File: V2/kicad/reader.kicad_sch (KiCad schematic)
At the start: 88 parts, among them SW1 SSSS812201, U1 MLD-TF PUSH-H18, U2 MAX98357AETE+T, U3 MCP16301Hx-xCH, U4 TCAN1057AVDRQ1, U5 RJ-064-1, U6 STM32H523CET6, U7 ESD2CAN24-ES, Y1 16MHz

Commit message: in process of making pcb
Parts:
- removed R5: 560 R, Resistor_SMD:R_0603_1608Metric, symbol Device:R
- removed RC522: RFID RC522, UACS:PinSocket_1x08_P2.54mm_Vertical, symbol Connector:Conn_01x08_Socket
- removed SP_Conn1: P=1.25mm, easyeda2kicad:CONN-TH_530480210, symbol easyeda2kicad:530480210
- added R15: 560 R, Resistor_SMD:R_0402_1005Metric, symbol Device:R
- added RC1: RFID RC522, UACS:PinSocket_1x08_P2.54mm_Vertical, symbol easyeda2kicad:HXPM2.54-1X8PZCH11
- added SP_Conn1: P=1.25mm, easyeda2kicad:CONN-TH_0530470210, symbol easyeda2kicad:0530470210
- SW1: value SSSS812201 -> SW_Rezistance
- SW2: renamed from BOOT2; value SW2 -> SW_src
- TP3: renamed from WS; value TestPoint -> WS
- U1: renamed from U6; footprint LQFP48_STM -> STM32H523CET6:LQFP48_STM
- renumbered BOOT1 to BOOT2, C30 to C10, C29 to C11, C28 to C12, C7 to C13, C36 to C14, C37 to C15, C3 to C16, C2 to C17, C35 to C18, C34 to C19, C4 to C2, C33 to C20, C23 to C21, C14 to C22, C12 to C23, C15 to C24, C17 to C25, C16 to C3, C6 to C4, C13 to C5, C8 to C6, C5 to C7, C32 to C8, C31 to C9, D7 to D1, D6 to D2, D10 to D3, D9 to D4, D1 to D5, D3 to D6, D5 to D7, D4 to D8, D2 to D9, FB2 to FB1, R17 to R1, R23 to R10, R24 to R11, R26 to R12, R11 to R13, R4 to R14, R6 to R16, R7 to R17, R8 to R18, R12 to R19, R20 to R2, R13 to R20, R9 to R21, R19 to R3, R14 to R4, R15 to R5, R16 to R6, R10 to R7, R21 to R8, R22 to R9, TP9 to TP1, TP7 to TP2, TP6 to TP4, TP3 to TP5, TP2 to TP6, TP1 to TP7, TP4 to TP8, TP5 to TP9, U1 to U3, U7 to U5, U5 to U6, U3 to U7
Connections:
- net +3.3V: now also RC1.1
- net GND: now also USB-C1.SH (SHIELD), RC1.3; no longer USB-C1.S1 (SHIELD)
- net LED_G2: now also U1.40 (PB4); no longer U1.42 (PB6)
- net LED_R1: now also R15.1
- net LED_R2: now also U1.38 (PA15); no longer U1.41 (PB5)
- net RFID_IRQ: now also RC1.4
- net RFID_SS: now also RC1.8
- net SPI_MISO: now also RC1.5
- net SPI_MOSI: now also RC1.6
- net SPI_SCK: now also RC1.7
- net at Speaker1.1, U2.10 (OUTN): now also SP_Conn1.1
- net at Speaker1.2, U2.9 (OUTP): now also SP_Conn1.2
- net RFID_RST: now reaches U1.21 (PB10)
- net RFID_RST: now also RC1.2
- net at LED1.1 (A1): now also R15.2
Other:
- note added: "Warning: No net found for component SW1 pad 5 (no pin 5 in symbol). Warning: No net found for component USB-C1 pad B8 (no pin B8 in symbol). Warning: No net found for component SW1 pad 7 (no pin 7 in symbol). Warning: No net found for component SW1 pad 6 (no pin 6 in symbol). Warning: No net found for component SW1 pad 8 (no pin 8 in symbol). Warning: No net found for component USB-C1 pad A8 (no 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"

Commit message: pcb propably dones
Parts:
- added H4: MountingHole, MountingHole:ToolingHole_1.152mm, symbol Mechanical:MountingHole
- C1, C10, C11, C12, C13, C18, C19, C2, C20, C21, C22, C23, C24, C25, C3, C5, C6, C8, C9, FB1, R12, R13, R14, R15, R16, R17, R18, R19, R2, R20, R21, R3, R5, R6, R7: KiLib_Generator (none) -> SMD_2terminal_chip_molded
- RC1: JLCPCB (none) -> https://jlcpcb.com/partdetail/28187-2_54_1_8P/C27438; LCSC (none) -> C27438
- SW1: LCSC Part (none) -> C160878
- TP1, TP2, TP3, TP4, TP5: footprint (none) -> UACS:TestPoint_Drill-1mm
- TP6, TP7, TP8, TP9: footprint TestPoint:TestPoint_THTPad_D1.0mm_Drill0.5mm -> UACS:TestPoint_Drill-1mm; now in the parts list
- U7: KiLib_Generator (none) -> package/gullwing
- Y1: KiLib_Generator (none) -> crystal_resonator_oscillator
- renumbered BOOT2 to BOOT1, SP_Conn1 to SP_Con1
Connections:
- net LED_G1: now also U1.40 (PB4); no longer U1.12 (PA2)
- net LED_G2: now also U1.42 (PB6); no longer U1.40 (PB4)
- net LED_R1: now also U1.38 (PA15); no longer U1.11 (PA1)
- net LED_R2: now also U1.41 (PB5); no longer U1.38 (PA15)
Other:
- note removed: "Warning: No net found for component SW1 pad 5 (no pin 5 in symbol). Warning: No net found for component USB-C1 pad B8 (no pin B8 in symbol). Warning: No net found for component SW1 pad 7 (no pin 7 in symbol). Warning: No net found for component SW1 pad 6 (no pin 6 in symbol). Warning: No net found for component SW1 pad 8 (no pin 8 in symbol). Warning: No net found for component USB-C1 pad A8 (no 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"

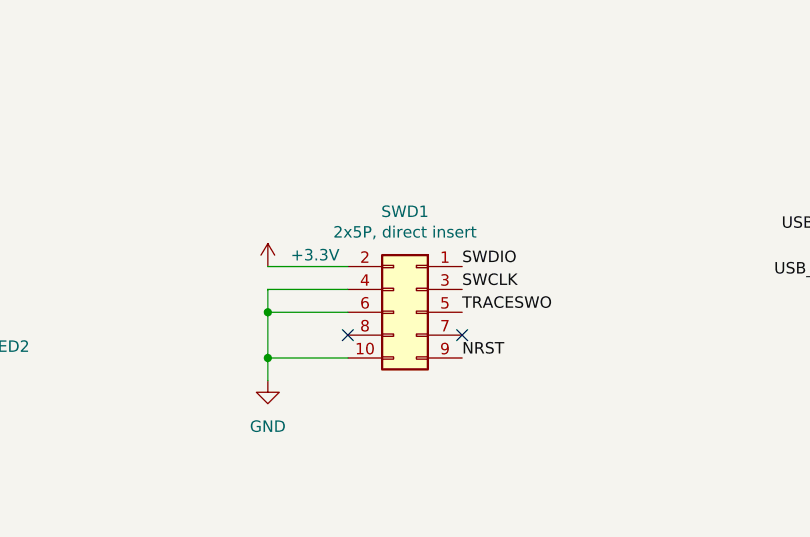
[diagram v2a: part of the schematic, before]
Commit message: changed debug connector to male, fixed 3d models not showing, moved sdcard slot invards by 2.3mm
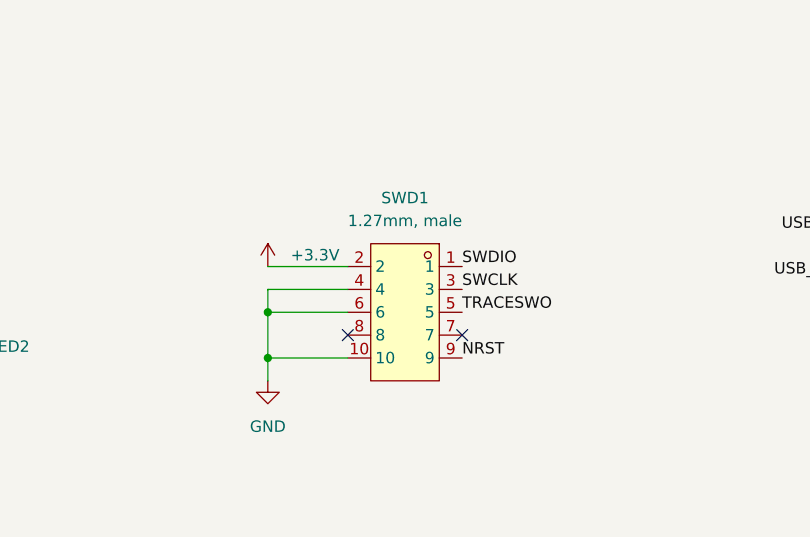
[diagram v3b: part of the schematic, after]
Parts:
- removed SWD1: 2x5P, direct insert, UACS:PinSocket_2x05_P1.27mm_Vertical, symbol Connector_Generic:Conn_02x05_Odd_Even
- added SWD1: 1.27mm, male, easyeda2kicad:CONN-TH_IDC1.27-UP1S-5A, symbol easyeda2kicad:IDC1.27-UP1S-5A
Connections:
- net +3.3V: now also SWD1.2
- net GND: now also SWD1.10, SWD1.4, SWD1.6
- net NRST: now also SWD1.9
- net SWCLK: now also SWD1.3
- net SWDIO: now also SWD1.1
- net TRACESWO: now also SWD1.5
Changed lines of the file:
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@@
+	)
+	(symbol
+		(lib_id "easyeda2kicad:IDC1.27-UP1S-5A")
+		(at 95.25 256.54 0)
+		(mirror y)
+		(unit 1)
+		(body_style 1)
+		(exclude_from_sim no)
+		(in_bom yes)
+		(on_board yes)
+		(in_pos_files yes)
+		(dnp no)
+		(fields_autoplaced yes)
+		(property "Reference" "SWD1"
+			(at 95.25 243.84 0)
+			(show_name no)
+			(do_not_autoplace no)
+			(effects
+				(font
+					(size 1.27 1.27)
+				)
+			)
+		)
+		(property "Value" "1.27mm, male"
+			(at 95.25 246.38 0)
+			(show_name no)
+			(do_not_autoplace no)
+			(effects
+				(font
+					(size 1.27 1.27)
+				)
+			)
+		)
+		(property "Footprint" "easyeda2kicad:CONN-TH_IDC1.27-UP1S-5A"
+			(at 95.25 269.24 0)
+			(hide yes)
+			(show_name no)
+			(do_not_autoplace no)
+			(effects
+				(font
+					(size 1.27 1.27)
+				)
+			)
+		)
+		(property "Datasheet" "https://www.lcsc.com/datasheet/C22392234.pdf"
+			(at 95.25 271.78 0)
+			(hide yes)
+			(show_name no)
+			(do_not_autoplace no)
+			(effects
+				(font
+					(size 1.27 1.27)
+				)
+			)
+		)
+		(property "Description" ""
+			(at 95.25 256.54 0)
+			(hide yes)
+			(show_name no)
+			(do_not_autoplace no)
+			(effects
+				(font
+					(size 1.27 1.27)
+				)
+			)
+		)
+		(property "Manufacturer" "XYECONN(辛译)"
+			(at 95.25 274.32 0)
+			(hide yes)
+			(show_name no)
+			(do_not_autoplace no)
+			(effects
+				(font
+					(size 1.27 1.27)
+				)
+			)
+		)
+		(property "MPN" "IDC1.27-UP1S-5A"
+			(at 95.25 276.86 0)
+			(hide yes)
+			(show_name no)
+			(do_not_autoplace no)
+			(effects
+				(font
+					(size 1.27 1.27)
+				)
+			)
+		)
+		(property "LCSC Part" "C22392234"
+			(at 95.25 279.4 0)
+			(hide yes)
+			(show_name no)
+			(do_not_autoplace no)
+			(effects
+				(font
+					(size 1.27 1.27)
+				)
+			)
+		)
+		(pin "2"
+		)
+		(pin "1"
+		)
+		(pin "7"
+		)
+		(pin "3"
+		)
+		(pin "5"
+		)
+		(pin "4"
+		)
+		(pin "8"
+		)
+		(pin "10"
+		)
+		(pin "6"
+		)
+		(pin "9"
+		)
+		(instances
+			(project "reader"
+				(path "/6275a1a7-d424-4390-b849-2e49b1a9780b"
+					(reference "SWD1")
+					(unit 1)
+				)
+			)
+		)
 	)
 	(symbol
@@
 					(unit 1)
 				)
-			)
-		)
-	)
-	(symbol
-		(lib_id "Connector_Generic:Conn_02x05_Odd_Even")
-		(at 96.52 256.54 0)
-		(mirror y)
-		(unit 1)
-		(body_style 1)
-		(exclude_from_sim no)
-		(in_bom yes)
-		(on_board yes)
-		(in_pos_files yes)
-		(dnp no)
-		(property "Reference" "SWD1"
-			(at 95.25 245.364 0)
-			(show_name no)
-			(do_not_autoplace no)
-			(effects
-				(font
-					(size 1.27 1.27)
-				)
-			)
-		)
-		(property "Value" "2x5P, direct insert"
-			(at 95.25 247.65 0)
-			(show_name no)
-			(do_not_autoplace no)
-			(effects
-				(font
-					(size 1.27 1.27)
-				)
-			)
-		)
-		(property "Footprint" "UACS:PinSocket_2x05_P1.27mm_Vertical"
-			(at 96.52 256.54 0)
-			(hide yes)
-			(show_name no)
-			(do_not_autoplace no)
-			(effects
-				(font
-					(size 1.27 1.27)
-				)
-			)
-		)
-		(property "Datasheet" "https://jlcpcb.com/api/file/downloadByFileSystemAccessId/8588891463094841344"
-			(at 96.52 256.54 0)
-			(hide yes)
-			(show_name no)
-			(do_not_autoplace no)
-			(effects
-				(font
-					(size 1.27 1.27)
-				)
-			)
-		)
-		(property "Description" "Generic connector, double row, 02x05, odd/even pin numbering scheme (row 1 odd numbers, row 2 even numbers), script generated (kicad-library-utils/schlib/autogen/connector/)"
-			(at 96.52 256.54 0)
-			(hide yes)
-			(show_name no)
-			(do_not_autoplace no)
-			(effects
-				(font
-					(size 1.27 1.27)
-				)
-			)
-		)
-		(property "Note" ""
-			(at 96.52 256.54 0)
-			(hide yes)
-			(show_name no)
-			(do_not_autoplace no)
-			(effects
-				(font
-					(size 1.27 1.27)
-				)
-			)
-		)
-		(property "JLCPCB" "https://jlcpcb.com/partdetail/Hoauc-2343U205CNG1SNT01/C350287"
-			(at 96.52 256.54 0)
-			(hide yes)
-			(show_name no)
-			(do_not_autoplace no)
-			(effects
-				(font
-					(size 1.27 1.27)
-				)
-			)
-		)
-		(property "LCSC" "C350287"
-			(at 96.52 256.54 0)
-			(hide yes)
-			(show_name no)
-			(do_not_autoplace no)
-			(effects
-				(font
-					(size 1.27 1.27)
-				)
-			)
-		)
-		(property "Field5" ""
-			(at 96.52 256.54 0)
-			(hide yes)
-			(show_name no)
-			(do_not_autoplace no)
-			(effects
-				(font
-					(size 1.27 1.27)
-				)
-			)
-		)
-		(property "Field6" ""
-			(at 96.52 256.54 0)
-			(hide yes)
-			(show_name no)
-			(do_not_autoplace no)
-			(effects
-				(font
-					(size 1.27 1.27)
-				)
-			)
-		)
-		(pin "5"
-		)
-		(pin "2"
-		)
-		(pin "1"
-		)
-		(pin "6"
-		)
-		(pin "3"
-		)
-		(pin "4"
-		)
-		(pin "9"
-		)
-		(pin "7"
-		)
-		(pin "8"
-		)
-		(pin "10"
-		)
-		(instances
-			(project "reader"
-				(path "/6275a1a7-d424-4390-b849-2e49b1a9780b"
-					(reference "SWD1")
-					(unit 1)
-				)

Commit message: final touches
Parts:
- removed H4: MountingHole, MountingHole:ToolingHole_1.152mm, symbol Mechanical:MountingHole
- removed SWD1: 1.27mm, male, easyeda2kicad:CONN-TH_IDC1.27-UP1S-5A, symbol easyeda2kicad:IDC1.27-UP1S-5A
- added SWD1: 1.27mm, male, easyeda2kicad:IDC-TH_10P-P1.27-X1270WV-2X05A-6TV01, symbol easyeda2kicad:X1270WV-2X05B-6TV01
- renumbered SP_Con1 to Speaker2
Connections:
- net +3.3V: now also SWD1.2
- net GND: now also SWD1.10, SWD1.4, SWD1.6
- net NRST: now also SWD1.9
- net SWCLK: now also SWD1.3
- net SWDIO: now also SWD1.1
- net TRACESWO: now also SWD1.5
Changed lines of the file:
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@@
 	)
 	(symbol
-		(lib_id "Mechanical:MountingHole")
-		(at 137.16 186.69 0)
-		(mirror y)
-		(unit 1)
-		(body_style 1)
-		(exclude_from_sim yes)
-		(in_bom no)
-		(on_board yes)
-		(in_pos_files yes)
-		(dnp no)
-		(property "Reference" "H4"
-			(at 134.62 185.4199 0)
-			(show_name no)
-			(do_not_autoplace no)
-			(effects
-				(font
-					(size 1.27 1.27)
-				)
-				(justify left)
-			)
-		)
-		(property "Value" "MountingHole"
-			(at 134.62 187.9599 0)
-			(show_name no)
-			(do_not_autoplace no)
-			(effects
-				(font
-					(size 1.27 1.27)
-				)
-				(justify left)
-			)
-		)
-		(property "Footprint" "MountingHole:ToolingHole_1.152mm"
-			(at 137.16 186.69 0)
-			(hide yes)
-			(show_name no)
-			(do_not_autoplace no)
-			(effects
-				(font
-					(size 1.27 1.27)
-				)
-			)
-		)
-		(property "Datasheet" ""
-			(at 137.16 186.69 0)
-			(hide yes)
-			(show_name no)
-			(do_not_autoplace no)
-			(effects
-				(font
-					(size 1.27 1.27)
-				)
-			)
-		)
-		(property "Description" "Mounting Hole without connection"
-			(at 137.16 186.69 0)
-			(hide yes)
-			(show_name no)
-			(do_not_autoplace no)
-			(effects
-				(font
-					(size 1.27 1.27)
-				)
-			)
-		)
-		(property "Note" ""
-			(at 137.16 186.69 0)
-			(hide yes)
-			(show_name no)
-			(do_not_autoplace no)
-			(effects
-				(font
-					(size 1.27 1.27)
-				)
-			)
-		)
-		(property "Field5" ""
-			(at 137.16 186.69 0)
-			(hide yes)
-			(show_name no)
-			(do_not_autoplace no)
-			(effects
-				(font
-					(size 1.27 1.27)
-				)
-			)
-		)
-		(property "Field6" ""
-			(at 137.16 186.69 0)
-			(hide yes)
-			(show_name no)
-			(do_not_autoplace no)
-			(effects
-				(font
-					(size 1.27 1.27)
-				)
-			)
-		)
-		(instances
-			(project "reader"
-				(path "/6275a1a7-d424-4390-b849-2e49b1a9780b"
-					(reference "H4")
-					(unit 1)
-				)
-			)
-		)
-	)
-	(symbol
 		(lib_id "power:VAA")
 		(at 187.96 109.22 0)
@@
 	)
 	(symbol
+		(lib_id "easyeda2kicad:X1270WV-2X05B-6TV01")
+		(at 95.25 256.54 0)
+		(mirror y)
+		(unit 1)
+		(body_style 1)
+		(exclude_from_sim no)
+		(in_bom yes)
+		(on_board yes)
+		(in_pos_files yes)
+		(dnp no)
+		(fields_autoplaced yes)
+		(property "Reference" "SWD1"
+			(at 95.25 243.84 0)
+			(show_name no)
+			(do_not_autoplace no)
+			(effects
+				(font
+					(size 1.27 1.27)
+				)
+			)
+		)
+		(property "Value" "1.27mm, male"
+			(at 95.25 246.38 0)
+			(show_name no)
+			(do_not_autoplace no)
+			(effects
+				(font
+					(size 1.27 1.27)
+				)
+			)
+		)
+		(property "Footprint" "easyeda2kicad:IDC-TH_10P-P1.27-X1270WV-2X05A-6TV01"
+			(at 95.25 269.24 0)
+			(hide yes)
+			(show_name no)
+			(do_not_autoplace no)
+			(effects
+				(font
+					(size 1.27 1.27)
+				)
+			)
+		)
+		(property "Datasheet" "https://www.lcsc.com/datasheet/C2962225.pdf"
+			(at 95.25 271.78 0)
+			(hide yes)
+			(show_name no)
+			(do_not_autoplace no)
+			(effects
+				(font
+					(size 1.27 1.27)
+				)
+			)
+		)
+		(property "Description" ""
+			(at 95.25 256.54 0)
+			(hide yes)
+			(show_name no)
+			(do_not_autoplace no)
+			(effects
+				(font
+					(size 1.27 1.27)
+				)
+			)
+		)
+		(property "Manufacturer" "XKB Connection(中国星坤)"
+			(at 95.25 274.32 0)
+			(hide yes)
+			(show_name no)
+			(do_not_autoplace no)
+			(effects
+				(font
+					(size 1.27 1.27)
+				)
+			)
+		)
+		(property "MPN" "X1270WV-2x05B-9TV01"
+			(at 95.25 276.86 0)
+			(hide yes)
+			(show_name no)
+			(do_not_autoplace no)
+			(effects
+				(font
+					(size 1.27 1.27)
+				)
+			)
+		)
+		(property "LCSC Part" "C2962225"
+			(at 95.25 279.4 0)
+			(hide yes)
+			(show_name no)
+			(do_not_autoplace no)
+			(effects
+				(font
+					(size 1.27 1.27)
+				)
+			)
+		)
+		(pin "8"
+		)
+		(pin "5"
+		)
+		(pin "1"
+		)
+		(pin "6"
+		)
+		(pin "3"
+		)
+		(pin "9"
+		)
+		(pin "4"
+		)
+		(pin "7"
+		)
+		(pin "2"
+		)
+		(pin "10"
+		)
+		(instances
+			(project "reader"
+				(path "/6275a1a7-d424-4390-b849-2e49b1a9780b"
+					(reference "SWD1")
+					(unit 1)
+				)
+			)
+		)
+	)
+	(symbol
 		(lib_id "Connector:TestPoint")
 		(at 248.92 270.51 0)
@@
 		(in_pos_files yes)
 		(dnp no)
-		(property "Reference" "SP_Con1"
+		(property "Reference" "Speaker2"
 			(at 354.33 69.596 0)
 			(show_name no)
@@
 			(project "reader"
 				(path "/6275a1a7-d424-4390-b849-2e49b1a9780b"
-					(reference "SP_Con1")
+					(reference "Speaker2")
 					(unit 1)
 				)
@@
 					(unit 1)
 				)
-			)
-		)
-	)
-	(symbol
-		(lib_id "easyeda2kicad:IDC1.27-UP1S-5A")
-		(at 95.25 256.54 0)
-		(mirror y)
-		(unit 1)
-		(body_style 1)
-		(exclude_from_sim no)
-		(in_bom yes)
-		(on_board yes)
-		(in_pos_files yes)
-		(dnp no)
-		(fields_autoplaced yes)
-		(property "Reference" "SWD1"
-			(at 95.25 243.84 0)
-			(show_name no)
-			(do_not_autoplace no)
-			(effects
-				(font
-					(size 1.27 1.27)
-				)
-			)
-		)
-		(property "Value" "1.27mm, male"
-			(at 95.25 246.38 0)
-			(show_name no)
-			(do_not_autoplace no)
-			(effects
-				(font
-					(size 1.27 1.27)
-				)
-			)
-		)
-		(property "Footprint" "easyeda2kicad:CONN-TH_IDC1.27-UP1S-5A"
-			(at 95.25 269.24 0)
-			(hide yes)
-			(show_name no)
-			(do_not_autoplace no)
-			(effects
-				(font
-					(size 1.27 1.27)
-				)
-			)
-		)
-		(property "Datasheet" "https://www.lcsc.com/datasheet/C22392234.pdf"
-			(at 95.25 271.78 0)
-			(hide yes)
-			(show_name no)
-			(do_not_autoplace no)
-			(effects
-				(font
-					(size 1.27 1.27)
-				)
-			)
-		)
-		(property "Description" ""
-			(at 95.25 256.54 0)
-			(hide yes)
-			(show_name no)
-			(do_not_autoplace no)
-			(effects
-				(font
-					(size 1.27 1.27)
-				)
-			)
-		)
-		(property "Manufacturer" "XYECONN(辛译)"
-			(at 95.25 274.32 0)
-			(hide yes)
-			(show_name no)
-			(do_not_autoplace no)
-			(effects
-				(font
-					(size 1.27 1.27)
-				)
-			)
-		)
-		(property "MPN" "IDC1.27-UP1S-5A"
-			(at 95.25 276.86 0)
-			(hide yes)
-			(show_name no)
-			(do_not_autoplace no)
-			(effects
-				(font
-					(size 1.27 1.27)
-				)
-			)
-		)
-		(property "LCSC Part" "C22392234"
-			(at 95.25 279.4 0)
-			(hide yes)
-			(show_name no)
-			(do_not_autoplace no)
-			(effects
-				(font
-					(size 1.27 1.27)
-				)
-			)
-		)
-		(pin "2"
-		)
-		(pin "1"
-		)
-		(pin "7"
-		)
-		(pin "3"
-		)
-		(pin "5"
-		)
-		(pin "4"
-		)
-		(pin "8"
-		)
-		(pin "10"
-		)
-		(pin "6"
-		)
-		(pin "9"
-		)
-		(instances
-			(project "reader"
-				(path "/6275a1a7-d424-4390-b849-2e49b1a9780b"
-					(reference "SWD1")
-					(unit 1)
-				)

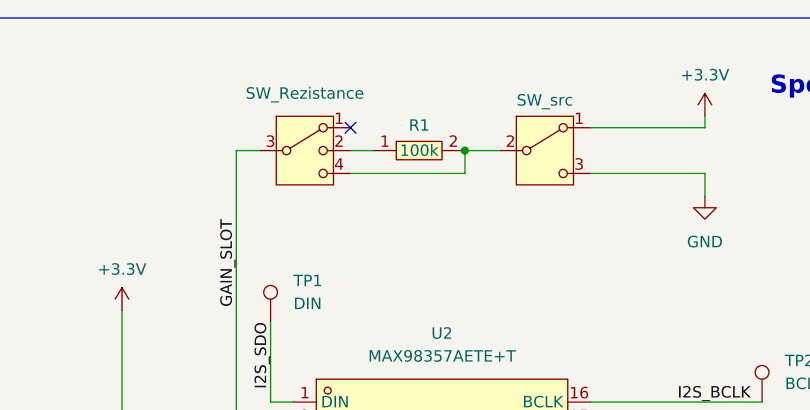
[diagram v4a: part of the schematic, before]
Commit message: added switch combination table at the back, swapped 2 positions of SW1... X <-> 100K so it better fits pcb
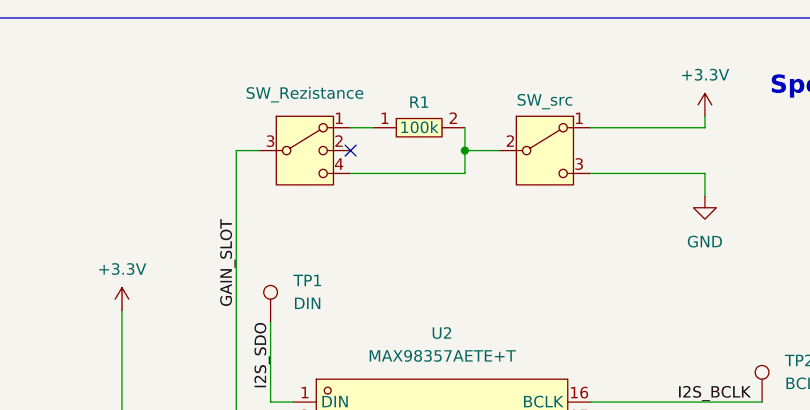
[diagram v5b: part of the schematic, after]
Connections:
- net at R1.1: now also SW1.1; no longer SW1.2
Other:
- moved on the sheet: R1
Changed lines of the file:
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@@
 	)
 	(junction
-		(at 327.66 30.48)
+		(at 226.06 229.87)
 		(diameter 0)
 		(color 0 0 0 0)
 	)
 	(junction
-		(at 226.06 229.87)
+		(at 327.66 30.48)
 		(diameter 0)
 		(color 0 0 0 0)
@@
 	)
 	(no_connect
+		(at 314.96 30.48)
+	)
+	(no_connect
 		(at 88.9 259.08)
 	)
@@
 	)
 	(no_connect
-		(at 314.96 27.94)
-	)
-	(no_connect
 		(at 308.61 68.58)
 	)
@@
 	(wire
 		(pts
+			(xy 327.66 27.94) (xy 327.66 30.48)
+		)
+		(stroke
+			(width 0)
+			(type default)
+		)
+	)
+	(wire
+		(pts
 			(xy 227.33 129.54) (xy 229.87 129.54)
 		)
@@
 	(wire
 		(pts
-			(xy 317.5 30.48) (xy 314.96 30.48)
-		)
-		(stroke
-			(width 0)
-			(type default)
-		)
-	)
-	(wire
-		(pts
 			(xy 194.31 124.46) (xy 204.47 124.46)
 		)
@@
 	(wire
 		(pts
+			(xy 317.5 27.94) (xy 314.96 27.94)
+		)
+		(stroke
+			(width 0)
+			(type default)
+		)
+	)
+	(wire
+		(pts
 			(xy 81.28 106.68) (xy 81.28 125.73)
 		)
@@
 	(symbol
 		(lib_id "easyeda2kicad:RC1206JR-07100KL")
-		(at 322.58 30.48 0)
+		(at 322.58 27.94 0)
 		(unit 1)
 		(body_style 1)
@@
 		(dnp no)
 		(property "Reference" "R1"
-			(at 322.58 27.686 0)
+			(at 322.58 25.146 0)
 			(show_name no)
 			(do_not_autoplace no)
@@
 		)
 		(property "Value" "RC1206JR-07100KL"
-			(at 322.58 26.924 0)
+			(at 322.58 24.384 0)
 			(hide yes)
 			(show_name no)
@@
 		)
 		(property "Footprint" "easyeda2kicad:R1206"
-			(at 322.58 38.1 0)
+			(at 322.58 35.56 0)
 			(hide yes)
 			(show_name no)
@@
 		)
 		(property "Datasheet" "https://lcsc.com/product-detail/Chip-Resistor-Surface-Mount_100KR-104-5_C136470.html"
-			(at 322.58 40.64 0)
+			(at 322.58 38.1 0)
 			(hide yes)
 			(show_name no)
@@
 		)
 		(property "Description" "100k"
-			(at 322.58 30.48 0)
+			(at 322.58 27.94 0)
 			(show_name no)
 			(do_not_autoplace no)
@@
 		)
 		(property "Manufacturer" "YAGEO(国巨)"
-			(at 322.58 43.18 0)
+			(at 322.58 40.64 0)
 			(hide yes)
 			(show_name no)
@@
 		)
 		(property "MPN" "RC1206JR-07100KL"
-			(at 322.58 45.72 0)
+			(at 322.58 43.18 0)
 			(hide yes)
 			(show_name no)
@@
 		)
 		(property "LCSC Part" "C136470"
-			(at 322.58 48.26 0)
+			(at 322.58 45.72 0)
 			(hide yes)
 			(show_name no)
